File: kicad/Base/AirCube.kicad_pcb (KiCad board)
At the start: 2 copper layers, 45 x 45 mm, 52 parts, among them P1 USB_C_Plug_USB2.0, Q1 BSS138, U10 ENS210, U2 ENS161, U5 AP2120, U6 AP2205, U7 ESP32-H2-MINI-1

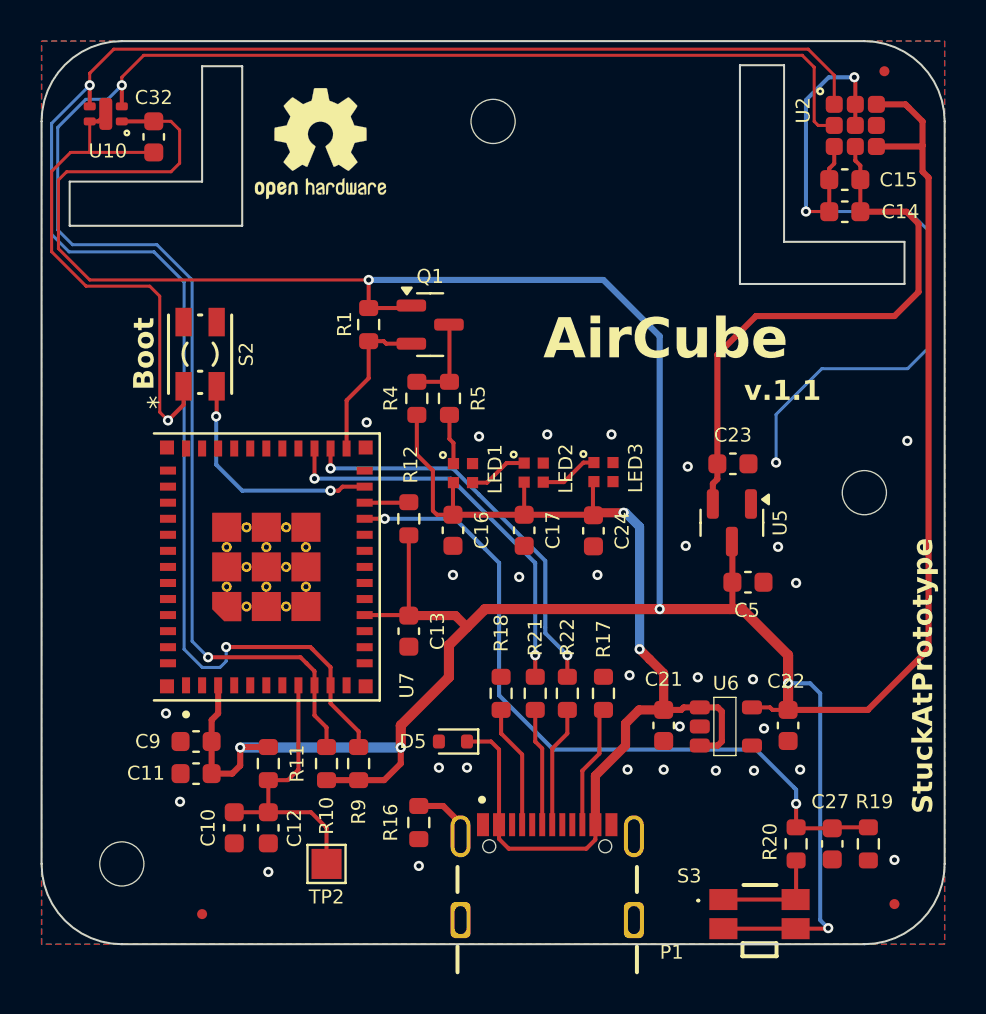
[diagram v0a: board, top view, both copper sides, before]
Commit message: Route local power stages and join regulator inputs
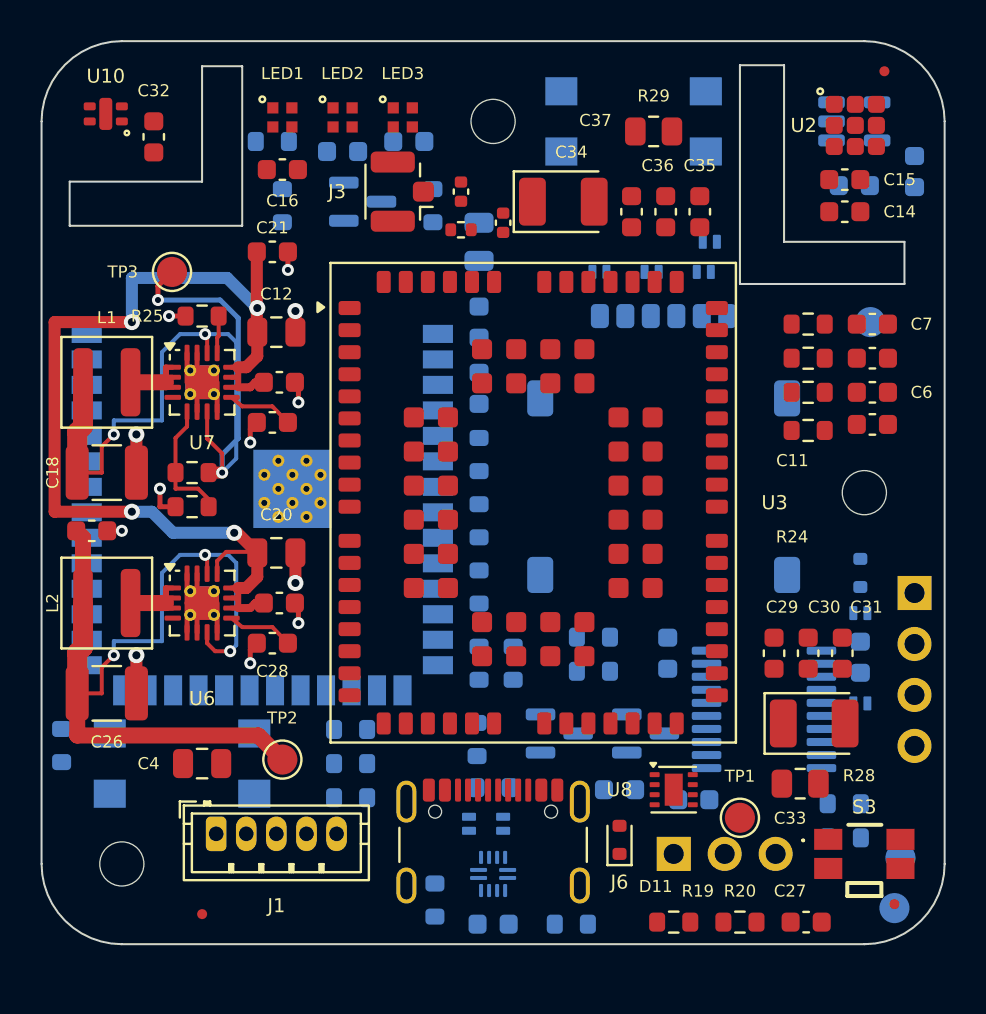
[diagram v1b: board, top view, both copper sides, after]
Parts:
- removed D5: TPD1E10B06, Diode_SMD:D_SOD-523
- removed P1: USB_C_Plug_USB2.0, kicad_reformed_custom_IC:GCT_USB4105-GF-A
- removed R17, R18: 5K1, Resistor_SMD:R_0603_1608Metric
- removed S2: SWITCH_0SMTRLFS, kicad_reformed_custom_IC:SWITCH_0SMTRLFS
- added C1: 10uF, Capacitor_SMD:C_0805_2012Metric, B.Cu at (45.8, 51.0)
- added C18: 22uF, Capacitor_SMD:C_1210_3225Metric, F.Cu at (27.2, 62.5)
- added C19: 3.3nF, Capacitor_SMD:C_0603_1608Metric, F.Cu at (35.5, 60.0)
- added C2: 0.1uF, Capacitor_SMD:C_0603_1608Metric, B.Cu at (45.8, 55.0)
- added C20: 10uF, Capacitor_SMD:C_0805_2012Metric, F.Cu at (35.7, 66.5)
- added C25: 100nF, Capacitor_SMD:C_0603_1608Metric, F.Cu at (35.9, 69.0)
- added C26: 22uF, Capacitor_SMD:C_1210_3225Metric, F.Cu at (27.2, 73.5)
- added C28: 3.3nF, Capacitor_SMD:C_0603_1608Metric, F.Cu at (35.5, 71.0)
- added C29: 100nF, Capacitor_SMD:C_0603_1608Metric, F.Cu at (60.5, 71.5)
- added C3: 1uF, Capacitor_SMD:C_0603_1608Metric, B.Cu at (45.8, 58.3)
- added C30: 33pF, Capacitor_SMD:C_0603_1608Metric, F.Cu at (62.2, 71.5)
- added C31: 10pF, Capacitor_SMD:C_0603_1608Metric, F.Cu at (63.9, 71.5)
- added C33: 100uF, Capacitor_Tantalum_SMD:CP_EIA-3528-21_Kemet-B, F.Cu at (62.5, 75.0)
- added C34: 100uF, Capacitor_Tantalum_SMD:CP_EIA-3528-21_Kemet-B, F.Cu at (50.0, 49.0)
- added C35: 100nF, Capacitor_SMD:C_0603_1608Metric, F.Cu at (56.8, 49.5)
- added C36: 33pF, Capacitor_SMD:C_0603_1608Metric, F.Cu at (55.1, 49.5)
- added C37: 10pF, Capacitor_SMD:C_0603_1608Metric, F.Cu at (53.4, 49.5)
- added C38: DNP, Capacitor_SMD:C_0402_1005Metric, F.Cu at (47.0, 50.0)
- added C39: DNP, Capacitor_SMD:C_0402_1005Metric, F.Cu at (44.9, 48.5)
- added C4: 10uF, Capacitor_SMD:C_0805_2012Metric, F.Cu at (32.0, 77.0)
- added C40: 100nF, Capacitor_SMD:C_0603_1608Metric, B.Cu at (46.5, 85.0)
- added C41: 1uF, Capacitor_SMD:C_0603_1608Metric, B.Cu at (52.8, 78.3)
- added C42: 10nF, Capacitor_SMD:C_0603_1608Metric, B.Cu at (56.5, 78.8)
- added C6: 33pF, Capacitor_SMD:C_0603_1608Metric, F.Cu at (65.4, 58.5)
- added C7: 33pF, Capacitor_SMD:C_0603_1608Metric, F.Cu at (65.4, 55.1)
- added C8: 100nF, Capacitor_SMD:C_0603_1608Metric, B.Cu at (64.8, 71.7)
- added D1: PESD3V3U1UL, Diode_SMD:D_SOD-882, B.Cu at (57.0, 52.5)
- added D10: PESD3V3U1UL, Diode_SMD:D_SOD-882, B.Cu at (47.0, 80.0)
- added D11: TPD1E10B06DYAR, Diode_SMD:D_SOD-523, F.Cu at (52.8, 80.8)
- added D2: PESD3V3U1UL, Diode_SMD:D_SOD-882, B.Cu at (54.4, 52.5)
- added D3: PESD3V3U1UL, Diode_SMD:D_SOD-882, B.Cu at (51.8, 52.5)
- added D4: PESD3V3U1UL, Diode_SMD:D_SOD-882, B.Cu at (57.3, 51.0)
- added D6: PESD3V3U1UL, Diode_SMD:D_SOD-882, B.Cu at (64.8, 69.5)
- added D7: PESD3V3U1UL, Diode_SMD:D_SOD-882, B.Cu at (64.8, 74.0)
- added D8: TPD1E10B06DYAR, Diode_SMD:D_SOD-523, B.Cu at (64.8, 67.5)
- added D9: PESD3V3U1UL, Diode_SMD:D_SOD-882, B.Cu at (45.3, 80.0)
- added J1: SPS30_UART, Connector_JST:JST_ZH_B5B-ZR_1x05_P1.50mm_Vertical, F.Cu at (32.7, 80.5)
- added J2: SIM_Card, AirCube_Recovered:nanoSIM_GCT_SIM8060-6-0-14-00_GroundedShell, B.Cu at (55.0, 61.5)
- added J3: LTE_ANT_UFL, Connector_Coaxial:U.FL_Hirose_U.FL-R-SMT-1_Vertical, F.Cu at (41.5, 48.5)
- added J4: MCU_UART_3V3, Connector_PinHeader_2.54mm:PinHeader_1x03_P2.54mm_Vertical, B.Cu at (55.5, 81.5)
- added J5: MODEM_USB_SERVICE, Connector_PinHeader_2.54mm:PinHeader_1x04_P2.54mm_Vertical, B.Cu at (67.5, 68.5)
- added J6: USB_C_Receptacle_USB2.0_14P, Connector_USB:USB_C_Receptacle_GCT_USB4105-xx-A_16P_TopMnt_Horizontal, F.Cu at (46.5, 82.0)
- added L1: 2.2uH, Inductor_SMD:L_Coilcraft_XAL4020-XXX, F.Cu at (27.2, 58.0)
- added L2: 2.2uH, Inductor_SMD:L_Coilcraft_XAL4020-XXX, F.Cu at (27.2, 69.0)
- added Q2: MMBT3904, Package_TO_SOT_SMD:SOT-23, B.Cu at (49.8, 75.5)
- added Q3: MMBT3904, Package_TO_SOT_SMD:SOT-23, B.Cu at (54.1, 75.5)
- added R13: 120k, Resistor_SMD:R_0603_1608Metric, B.Cu at (64.0, 80.7)
- added R14: 0, Resistor_SMD:R_0603_1608Metric, F.Cu at (62.2, 55.1)
- added R15: 0, Resistor_SMD:R_0603_1608Metric, F.Cu at (62.2, 56.8)
- added R2: 10k, Resistor_SMD:R_0603_1608Metric, B.Cu at (45.8, 61.6)
- added R23: 0, Resistor_SMD:R_0603_1608Metric, F.Cu at (62.2, 58.5)
- added R24: 15k, Resistor_SMD:R_0603_1608Metric, F.Cu at (62.2, 60.4)
- added R25: 100k, Resistor_SMD:R_0603_1608Metric, F.Cu at (32.0, 54.7)
- added R26: 100k, Resistor_SMD:R_0603_1608Metric, F.Cu at (31.5, 64.2)
- added R27: 374k, Resistor_SMD:R_0603_1608Metric, F.Cu at (31.5, 62.5)
- added R28: 0, Resistor_SMD:R_0805_2012Metric, F.Cu at (61.8, 78.0)
- added R29: 0, Resistor_SMD:R_0805_2012Metric, F.Cu at (54.5, 45.5)
- added R3: 10k, Resistor_SMD:R_0603_1608Metric, B.Cu at (25.0, 76.1)
- added R30: 0, Resistor_SMD:R_0402_1005Metric, F.Cu at (44.9, 50.4)
- added R31: 0, Resistor_SMD:R_0603_1608Metric, B.Cu at (39.4, 75.3)
- added R32: 0, Resistor_SMD:R_0603_1608Metric, B.Cu at (39.4, 77.0)
- added R33: 0, Resistor_SMD:R_0603_1608Metric, B.Cu at (39.4, 78.7)
- added R34: 887k, Resistor_SMD:R_0603_1608Metric, B.Cu at (50.4, 85.0)
- added R6: 47K, Resistor_SMD:R_0603_1608Metric, B.Cu at (46.5, 78.2)
- added R7: 47K, Resistor_SMD:R_0603_1608Metric, B.Cu at (51.5, 72.4)
- added R8: 4.7K, Resistor_SMD:R_0603_1608Metric, B.Cu at (45.7, 75.8)
- added SW1: RESET, Button_Switch_SMD:SW_SPST_TL3305A, B.Cu at (53.5, 45.0)
- added SW2: BOOT, Button_Switch_SMD:SW_SPST_TL3305A, B.Cu at (31.0, 77.0)
- added TP1: TP_5V, TestPoint:TestPoint_Pad_D1.5mm, F.Cu at (58.8, 79.7)
- added TP3: TP_MODEM_VBAT, TestPoint:TestPoint_Pad_D1.5mm, F.Cu at (30.5, 52.5)
- added TP4: TP_MODEM_1V8, TestPoint:TestPoint_Pad_D1.5mm, B.Cu at (66.5, 84.2)
- added TP5: TP_SIM_VDD, TestPoint:TestPoint_Pad_D1.5mm, B.Cu at (65.3, 55.0)
- added TP6: TP_GND, TestPoint:TestPoint_Pad_D1.5mm, B.Cu at (66.8, 81.7)
- added U1: ESP32-S3-WROOM-1U-N8, AirCube_Recovered:ESP32-S3-WROOM-1U_ThermalDrill0.30, B.Cu at (35.0, 64.0)
- added U11: TUSB320LAIRWBR, Package_DFN_QFN:Texas_X2QFN-12_1.6x1.6mm_P0.4mm, B.Cu at (46.5, 82.5)
- added U3: BG95-M3, RF_GSM:Quectel_BG95, F.Cu at (48.5, 64.0)
- added U4: TXS0108EPW, Package_SO:TSSOP-20_4.4x6.5mm_P0.65mm, B.Cu at (60.0, 74.3)
- added U8: TPS22975DSGR, AirCube_Recovered:TPS22975_DSG_TI_LandPattern, F.Cu at (55.5, 78.3)
- C10: value 1uF -> 33pF
- C11, C13: value 0.1uF -> 100nF
- C12: value 0.1uF -> 10uF; footprint Capacitor_SMD:C_0603_1608Metric -> Capacitor_SMD:C_0805_2012Metric
- C14, C15, C16, C21, C22, C27, C32: footprint Capacitor_SMD:C_0603_1608Metric -> AirCube_Recovered:C_0603_1608Metric
- C17, C23, C24, C5: footprint Capacitor_SMD:C_0603_1608Metric -> AirCube_Recovered:C_0603_1608Metric; moved to B.Cu
- C9: value 47uF -> 100nF; moved to B.Cu
- G***: footprint kicad_reformed_custom_IC:LOGO_6mm_microDMG -> AirCube_Recovered:AirCube_Logo_Documentation
- LED1, LED2, LED3: footprint custom_IC:IN-PI15_INL -> AirCube_Recovered:IN-PI15_INL
- Q1: footprint Package_TO_SOT_SMD:SOT-23 -> AirCube_Recovered:SOT-23; moved to B.Cu
- R1, R10, R16, R21, R22, R4, R5, R9: footprint Resistor_SMD:R_0603_1608Metric -> AirCube_Recovered:R_0603_1608Metric; moved to B.Cu
- R11: value 10K -> 4.7K; moved to B.Cu
- R12: value 10K -> 10k; moved to B.Cu
- R19, R20: footprint Resistor_SMD:R_0603_1608Metric -> AirCube_Recovered:R_0603_1608Metric
- REF** (x3): footprint Fiducial:Fiducial_0.5mm_Mask1.5mm -> AirCube_Recovered:Fiducial_0.5mm_Mask1.5mm
- REF**: footprint Symbol:OSHW-Logo2_7.3x6mm_SilkScreen -> AirCube_Recovered:OSHW_Logo_Documentation
- S3: footprint custom_IC:TL1016AAF220QG -> AirCube_Recovered:TL1016AAF220QG
- TP2: value TestPoint -> TP_3V3; footprint TestPoint:TestPoint_Pad_1.5x1.5mm -> TestPoint:TestPoint_Pad_D1.5mm
- U10: footprint kicad_reformed_custom_IC:ENS210 -> AirCube_Recovered:ENS210
- U2: footprint kicad_reformed_custom_IC:ENS161 -> AirCube_Recovered:ENS161
- U5: value AP2120 -> TLV75518PDBV; footprint Package_TO_SOT_SMD:SOT-23 -> Package_TO_SOT_SMD:SOT-23-5; moved to B.Cu
- U6: value AP2205 -> TPS62132; footprint kicad_reformed_custom_IC:AP2204 -> AirCube_Recovered:TPS6213x_RGT_ThermalDrill0.30
- U7: value ESP32-H2-MINI-1 -> TPS62130; footprint kicad_reformed_custom_IC:MODULE_ESP32-H2-MINI-1-H2 -> AirCube_Recovered:TPS6213x_RGT_ThermalDrill0.30
- moved C10 39.5 mm to (65.4, 56.8), turned to 0 degrees
- moved C11 37.9 mm to (65.4, 60.1), turned to 0 degrees
- moved C22 36.0 mm to (26.5, 65.4), turned to 0 degrees
- moved C21 30.6 mm to (35.5, 51.5), turned to 0 degrees
- moved U6 26.8 mm to (32.0, 69.0), turned to 0 degrees
- moved R12 25.9 mm to (64.0, 79.0), turned to 0 degrees
- moved C12 24.7 mm to (35.7, 55.5), turned to 0 degrees
- moved C9 23.9 mm to (55.2, 71.5), turned to 90 degrees
- moved C5 22.1 mm to (67.5, 47.5), turned to 90 degrees
- moved C24 21.5 mm to (42.3, 46.0), turned to 0 degrees
- moved C17 20.9 mm to (39.0, 46.5), turned to 0 degrees
- moved U5 20.9 mm to (64.5, 45.0), turned to 0 degrees
- moved LED3 20.3 mm to (42.0, 44.8)
- moved LED2 20.1 mm to (39.0, 44.8)
- moved C16 19.9 mm to (36.0, 47.4), turned to 0 degrees
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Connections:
- C10 pad 1: /CP_EN -> /SIM_CLK_CARD
- C11 pad 1: +3V3 -> /SIM_VDD
- C12 pad 1: /CP_EN -> +5VD
- C13 pad 1: +3V3 -> +5VD
- C27 pad 1: Net-(U7-IO11) -> /USER_BUTTON
- Q1 pad 2: Net-(Q1-S) -> /LED_DATA
- R1 pad 1: Net-(Q1-S) -> /LED_DATA
- R11 pad 1: +3V3 -> Net-(Q3-B)
- R11 pad 2: /CP_EN -> /MODEM_RESET_CTL
- R12 pad 1: Net-(U7-IO08) -> Net-(U4-OE)
- R12 pad 2: +3V3 -> /MODEM_VDD_1V8
- R19 pad 1: Net-(U7-IO11) -> /USER_BUTTON
- R20 pad 1: Net-(U7-IO11) -> /USER_BUTTON
- R21 pad 2: Net-(P1-D+) -> /MCU_USB_DP_CONN
- R22 pad 1: Net-(P1-D-) -> /MCU_USB_DM_CONN
- TP2 pad 1: /CP_EN -> +3V3
- U5 pad 1: GND -> +3V3
- U5 pad 2: +1V8 -> GND
- U6 pad 1: +5VD -> Net-(L2-Pad2)
- U6 pad 2: GND -> Net-(L2-Pad2)
- U6 pad 3: +5VD -> Net-(L2-Pad2)
- U6 pad 5: +3V3 -> GND
- U7 pad 1: GND -> Net-(L1-Pad2)
- U7 pad 10: /SDA -> +5VD
- U7 pad 11: GND -> +5VD
- U7 pad 12: unconnected-(U7-IO13-Pad12) -> +5VD
- U7 pad 13: unconnected-(U7-IO14-Pad13) -> /MODEM_SUPPLY_EN
- U7 pad 14: GND -> /MODEM_VBAT
- U7 pad 15: +3V3 -> GND
- U7 pad 16: unconnected-(U7-IO12-Pad16) -> GND
- U7 pad 17: unconnected-(U7-NC-Pad17) -> GND
- U7 pad 2: GND -> Net-(L1-Pad2)
- U7 pad 3: +3V3 -> Net-(L1-Pad2)
- U7 pad 5: unconnected-(U7-IO2-Pad5) -> Net-(U7-FB)
- U7 pad 6: unconnected-(U7-IO3-Pad6) -> GND
- U7 pad 7: unconnected-(U7-NC-Pad7) -> /MODEM_VBAT
- U7 pad 8: /CP_EN -> GND
- U7 pad 9: /SCL -> Net-(U7-SS/TR)
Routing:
- net +3V3: track 185.3 -> 42.7 mm, vias 6 -> 3
- net /SDA: track 88.8 -> 0.00 mm, vias 2 -> 0
- net /SCL: track 86.1 -> 0.00 mm, vias 2 -> 0
- net /MODEM_VBAT: track 0.00 -> 44.6 mm, vias 0 -> 4
- net GND: track 65.7 -> 28.1 mm, vias 33 -> 12
- net Net-(U7-IO11): track 36.5 -> 0.00 mm, vias 2 -> 0
- net +1V8: track 28.8 -> 0.00 mm
- net /USB_D+: track 19.9 -> 0.00 mm, vias 2 -> 0
- net /USB_D-: track 19.8 -> 0.00 mm, vias 2 -> 0
- net /CP_EN: track 14.2 -> 0.00 mm
- net Net-(U7-IO9): track 11.9 -> 0.00 mm, vias 2 -> 0
- net Net-(Q1-S): track 7.98 -> 0.00 mm
- net Net-(U7-FB): track 0.00 -> 6.32 mm
- net Net-(P1-VCONN): track 6.16 -> 0.00 mm
- net Net-(P1-CC): track 6.15 -> 0.00 mm
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- added copper zone on In1.Cu, net GND
- added copper zone on In2.Cu, net GND
- removed copper zone on B.Cu, net GND
- removed copper zone on F.Cu, net GND
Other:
- copper layers 2 -> 4

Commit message: Checkpoint cellular and PM2.5 design before manufacturer-specific routing
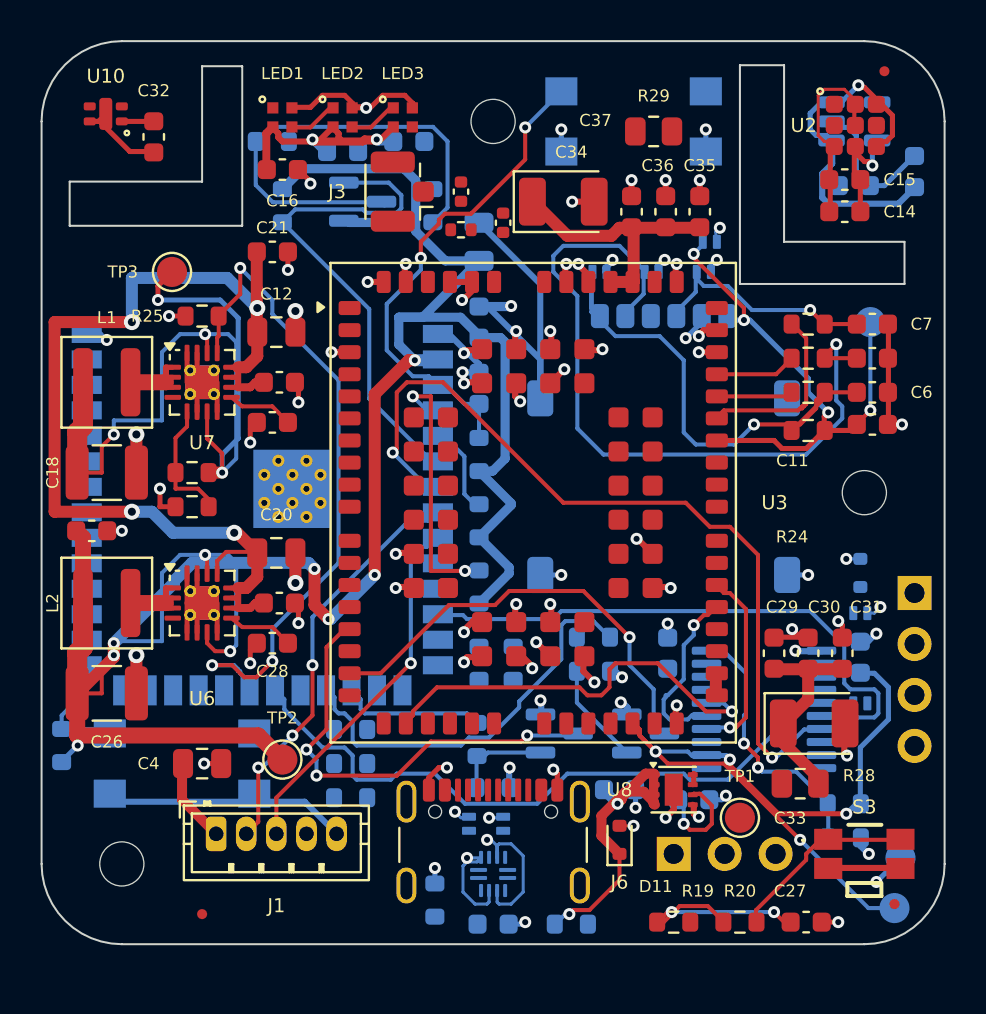
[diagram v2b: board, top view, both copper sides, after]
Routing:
- net GND: track 28.1 -> 187.8 mm, vias 12 -> 88
- net +3V3: track 42.7 -> 152.3 mm, vias 3 -> 10
- net /MODEM_RTS_3V3: track 0.00 -> 41.3 mm, vias 0 -> 2
- net /MODEM_VDD_1V8: track 0.00 -> 39.0 mm, vias 0 -> 4
- net /SIM_CLK_CARD: track 0.00 -> 38.1 mm, vias 0 -> 1
- net /MODEM_STATUS_3V3: track 0.00 -> 33.2 mm
- net /MODEM_SUPPLY_EN: track 1.87 -> 34.1 mm, vias 0 -> 3
- net /MODEM_CTS_3V3: track 0.00 -> 29.1 mm
- net /SIM_VDD: track 0.00 -> 27.7 mm, vias 0 -> 4
- net /SIM_DATA_CARD: track 0.00 -> 26.5 mm, vias 0 -> 1
- net /LED_DATA: track 0.00 -> 25.6 mm
- net Net-(U1-EN): track 0.00 -> 24.7 mm, vias 0 -> 2
- net Net-(Q1-D): track 0.00 -> 23.6 mm
- net /MODEM_PWRKEY: track 0.00 -> 22.6 mm, vias 0 -> 3
- net /MODEM_RESET_N: track 0.00 -> 22.1 mm, vias 0 -> 1
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
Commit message: got routing with 0 errors; some power errors visible
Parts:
- C8, C9: moved to F.Cu
- moved R32 13.9 mm to (46.2, 64.9), turned to 90 degrees
- moved R9 13.7 mm to (39.4, 77.0), turned to 0 degrees
- moved TP1 12.9 mm to (60.8, 67.0)
- moved R33 12.5 mm to (46.2, 68.2), turned to -90 degrees
- moved C9 12.4 mm to (65.4, 78.6), turned to 180 degrees
- moved R10 12.3 mm to (39.4, 78.7), turned to 0 degrees
- moved C8 9.37 mm to (58.2, 78.3)
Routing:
- net +3V3: track 152.3 -> 316.9 mm, vias 10 -> 23
- net /SDA: track 4.88 -> 141.5 mm, vias 0 -> 16
- net /MCU_DEBUG_RX: track 0.00 -> 116.0 mm, vias 0 -> 8
- net +5VD: track 71.6 -> 179.0 mm, vias 6 -> 13
- net /SCL: track 13.6 -> 117.6 mm, vias 2 -> 9
- net /MODEM_VBAT: track 44.6 -> 111.3 mm, vias 4 -> 8
- net /MCU_DEBUG_TX: track 0.00 -> 56.2 mm, vias 0 -> 1
- net /MODEM_TX_3V3: track 0.00 -> 52.8 mm, vias 0 -> 4
- net /MODEM_USB_VBUS: track 0.00 -> 40.2 mm, vias 0 -> 3
- net GND: track 187.8 -> 225.6 mm, vias 88 -> 98
- net /MODEM_RX_3V3: track 0.00 -> 37.0 mm, vias 0 -> 2
- net /MODEM_USB_DP_HOST: track 0.00 -> 34.1 mm
- net Net-(J6-SHIELD): track 0.00 -> 28.0 mm, vias 0 -> 6
- net /USER_BUTTON: track 11.1 -> 36.9 mm, vias 2 -> 4
- net /MODEM_USB_DM_HOST: track 0.00 -> 23.5 mm, vias 0 -> 2
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
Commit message: Finalize AirCube hardware and manufacturing package for fabrication review
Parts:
- moved C37 4.03 mm to (56.8, 47.3), turned to 0 degrees
- moved C36 1.82 mm to (56.8, 48.8), turned to 0 degrees
- moved C35 0.80 mm to (56.8, 50.3), turned to 0 degrees
- turned C34 to 180 degrees
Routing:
- net /MODEM_VBAT: track 111.3 -> 53.6 mm, vias 8 -> 9
- net /MODEM_RX_3V3: track 37.0 -> 61.8 mm, vias 2 -> 6
- net GND: track 225.6 -> 248.8 mm, vias 98 -> 97
- net +3V3: track 316.9 -> 305.1 mm, vias 23 -> 21
- net /MODEM_TXD_1V8: track 7.65 -> 18.5 mm
- net /MODEM_VBAT_RF: track 24.2 -> 14.7 mm
- net /SDA: track 141.5 -> 148.5 mm
- net /USER_BUTTON: track 36.9 -> 42.2 mm
- net /MODEM_USB_VBUS: track 40.2 -> 45.0 mm
- net +5VD: track 179.0 -> 183.3 mm, vias 13 -> 17
- net Net-(Q1-D): track 21.7 -> 19.2 mm
- net /SCL: track 117.6 -> 115.2 mm, vias 9 -> 12
- net Net-(LED1-DIN): track 4.96 -> 3.72 mm, vias 2 -> 1
- net /PM_TX: track 21.0 -> 22.2 mm, vias 4 -> 5
- net Net-(J6-CC1): track 21.1 -> 21.0 mm, vias 2 -> 1
- added copper zone on In2.Cu, net +5VD
- added copper zone on In2.Cu, net /MODEM_VBAT
- added copper zone on F.Cu, net /MODEM_VBAT_RF
